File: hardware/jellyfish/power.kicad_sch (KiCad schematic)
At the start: 17 parts, among them U1 VX7805-500, U2 MIC5317-3.3

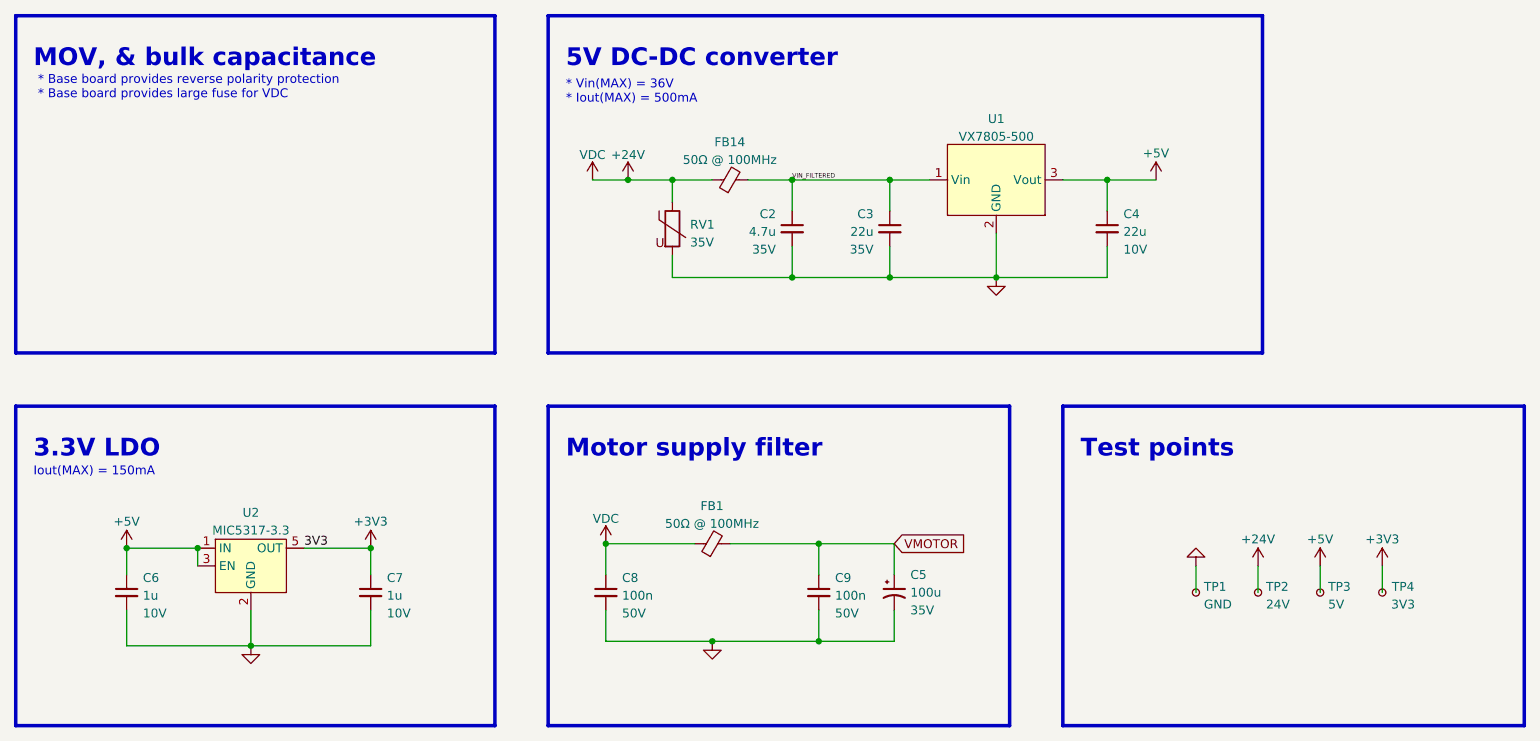
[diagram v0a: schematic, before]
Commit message: Update Jellyfish with some stuff from Starfish
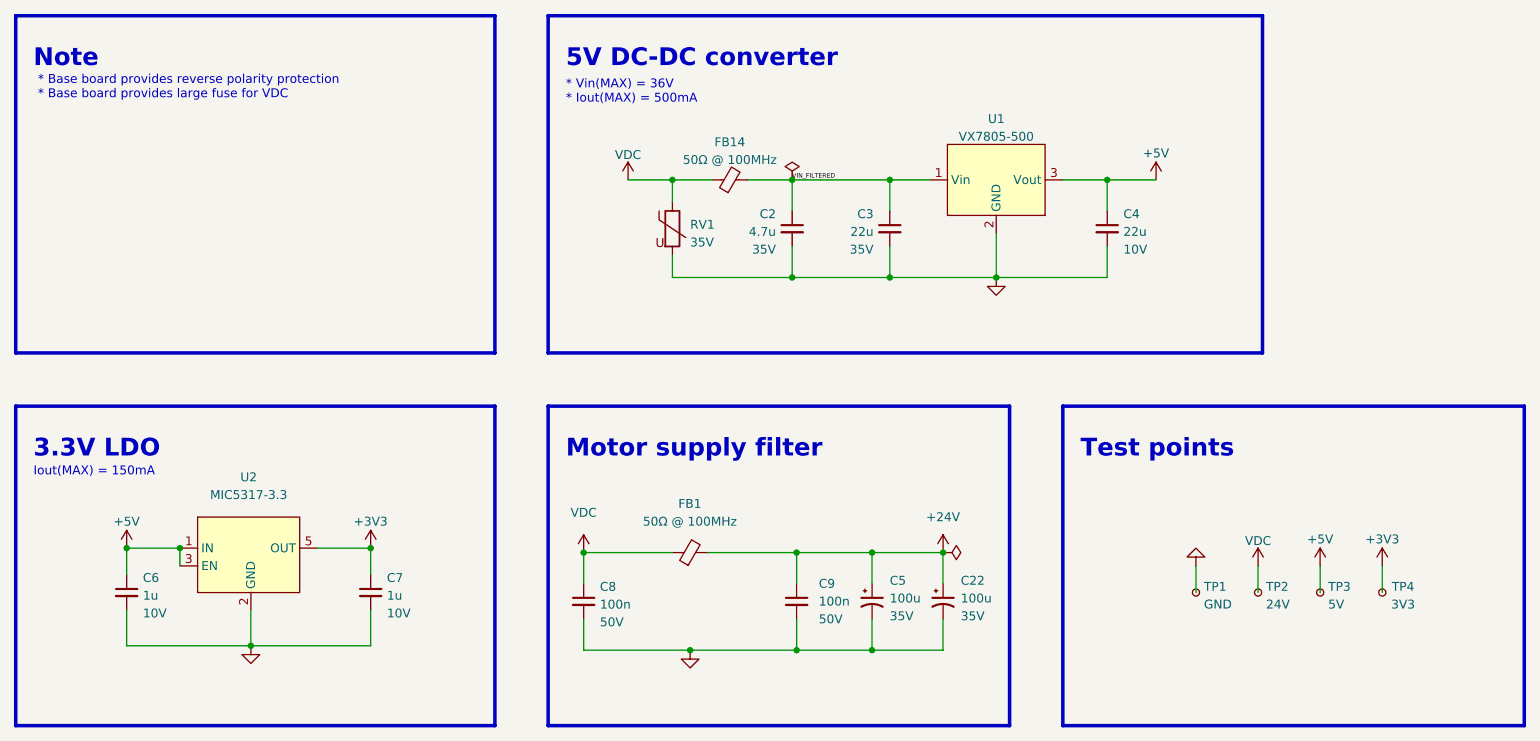
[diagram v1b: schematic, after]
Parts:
- added C22: 100u, Capacitor_SMD:CP_Elec_6.3x7.7, symbol Device:C_Polarized_Small_US
- C2, C3, C4: footprint Capacitor_SMD:C_0805_2012Metric_Pad1.18x1.45mm_HandSolder -> winterbloom:C_0805_HandSolder
- C6, C7, C8, C9: footprint Capacitor_SMD:C_0402_1005Metric_Pad0.74x0.62mm_HandSolder -> winterbloom:C_0402_HandSolder
- FB1, FB14: footprint Inductor_SMD:L_0603_1608Metric_Pad1.05x0.95mm_HandSolder -> winterbloom:L_0603_HandSolder
- RV1: footprint Resistor_SMD:R_0603_1608Metric_Pad0.98x0.95mm_HandSolder -> winterbloom:R_0603_HandSolder
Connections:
- net VMOTOR is gone; now on net +24V: C5.1, C9.1, FB1.2
- net +24V: now also C22.1; no longer C8.1, FB1.1, FB14.1, RV1.1, TP2.1
- net GND: now also C22.2
- new net VDC: C8.1, FB1.1, FB14.1, RV1.1, TP2.1
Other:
- note added: "Note"
- note removed: "MOV, & bulk capacitance"
- moved on the sheet: C5, C8, C9, FB1, U2
